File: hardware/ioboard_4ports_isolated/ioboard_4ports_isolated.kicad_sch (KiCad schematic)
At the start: 58 parts

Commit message: Finish IO-Board updates
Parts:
- C1, C10, C11, C12, C2, C3, C4, C5, C6, C7, C8, C9: value (none) -> 100nF; footprint (none) -> Capacitor_SMD:C_0603_1608Metric
- H1, H2, H3, H4: value (none) -> MountingHole; footprint (none) -> MountingHole:MountingHole_3.2mm_M3
- J1: value (none) -> Conn_02x06_Odd_Even; footprint (none) -> Connector_PinHeader_2.54mm:PinHeader_2x06_P2.54mm_Vertical
- J10, J2, J4, J8: value (none) -> XLR3; footprint (none) -> Connector_Audio:Jack_XLR_Neutrik_NC3FAAH_Horizontal
- J11, J3, J5, J9: value (none) -> XLR3; footprint (none) -> NC3FD-H:Jack_XLR_Neutrik_NC3FD-H_Horizontal
- J12, J13, J6, J7: value (none) -> Conn_01x03; footprint (none) -> Connector_PinHeader_2.54mm:PinHeader_1x03_P2.54mm_Vertical
- PS1, PS2: value (none) -> MEE1S0503SC; footprint (none) -> Converter_DCDC:Converter_DCDC_muRata_CRE1xxxxxx3C_THT
- R1, R11, R12, R17, R18, R2, R7, R8: value (none) -> 680R; footprint (none) -> Resistor_SMD:R_0603_1608Metric_Pad0.98x0.95mm_HandSolder
- R10, R19, R20, R9: value (none) -> 0R-DO_NOT_MOUNT; footprint (none) -> Resistor_SMD:R_0805_2012Metric_Pad1.20x1.40mm_HandSolder
- R13, R14, R3, R4: value (none) -> 0R; footprint (none) -> Resistor_SMD:R_0805_2012Metric_Pad1.20x1.40mm_HandSolder
- R15, R16, R5, R6: value (none) -> 120R; footprint (none) -> Resistor_SMD:R_0603_1608Metric_Pad0.98x0.95mm_HandSolder
- U1: value (none) -> M24C64-RMN6TP; footprint (none) -> Package_SO:SOIC-8_3.9x4.9mm_P1.27mm; LCSC C7562 -> C79988
- U2, U3: value (none) -> CRE1S0505DC; footprint (none) -> Converter_DCDC:Converter_DCDC_muRata_CRE1xxxxxxDC_THT
- U4, U5, U6, U7: value (none) -> ADM2483xRW; footprint (none) -> Package_SO:SOIC-16W_7.5x10.3mm_P1.27mm
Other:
- note added: "I2C EEPROM for board identification and configuration storage"
- note removed: "I2C EEPROM for board identification"

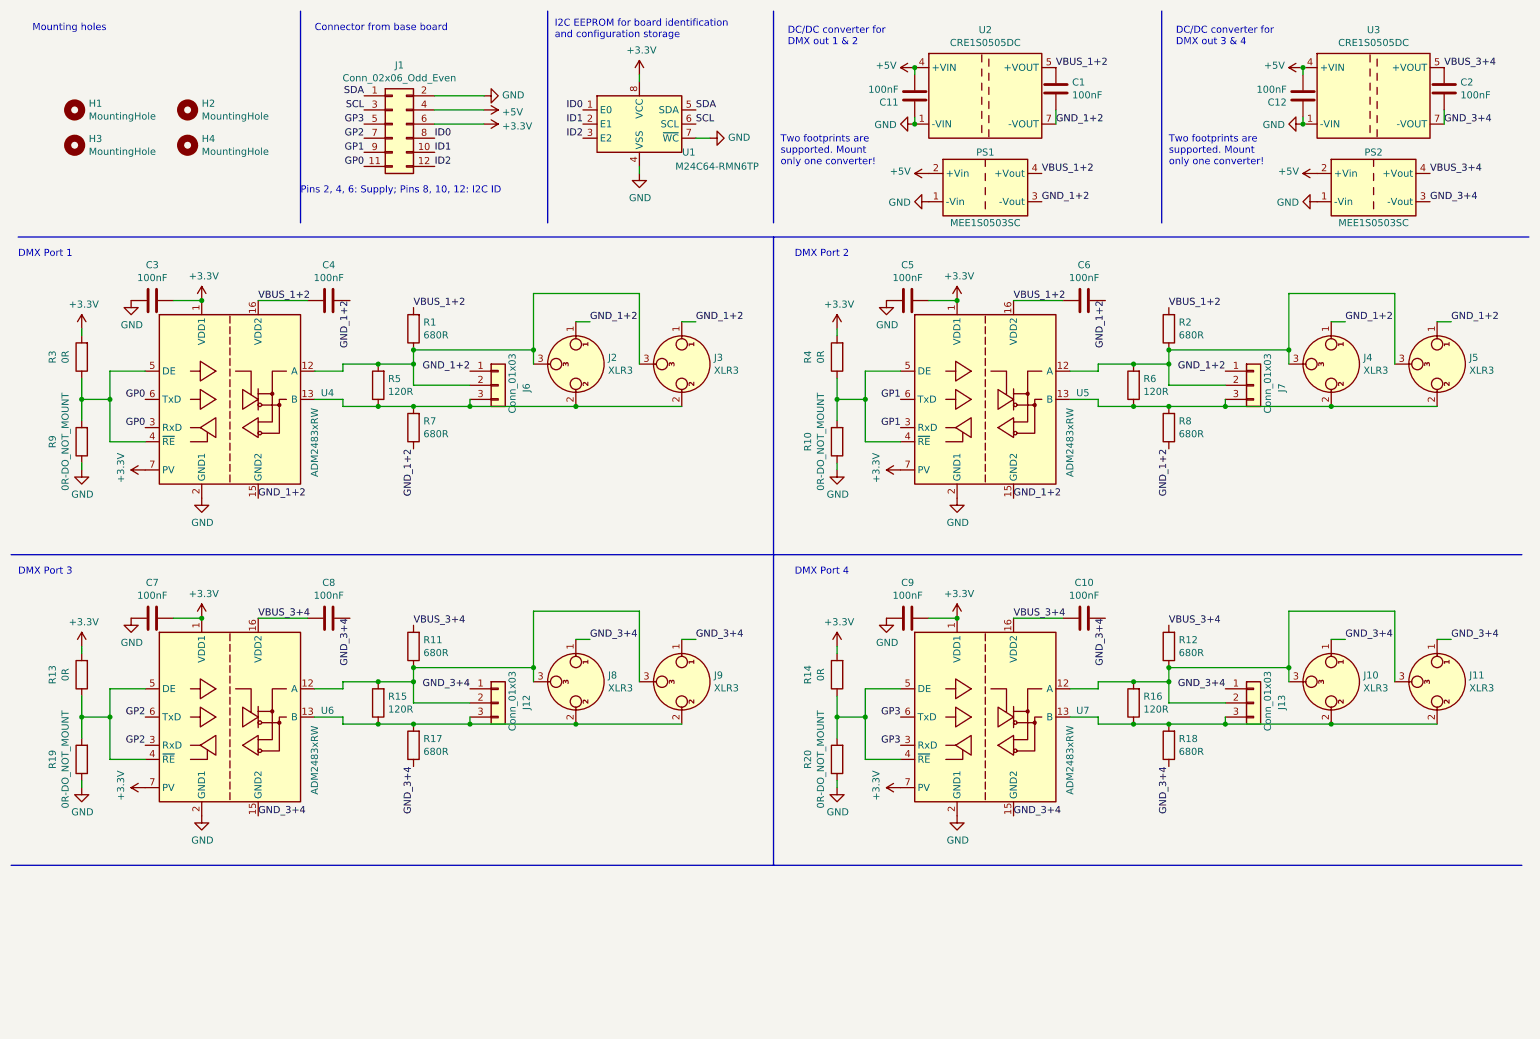
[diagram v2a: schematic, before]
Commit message: Add RJ45 jack to ioboard_4ports_isolated as well
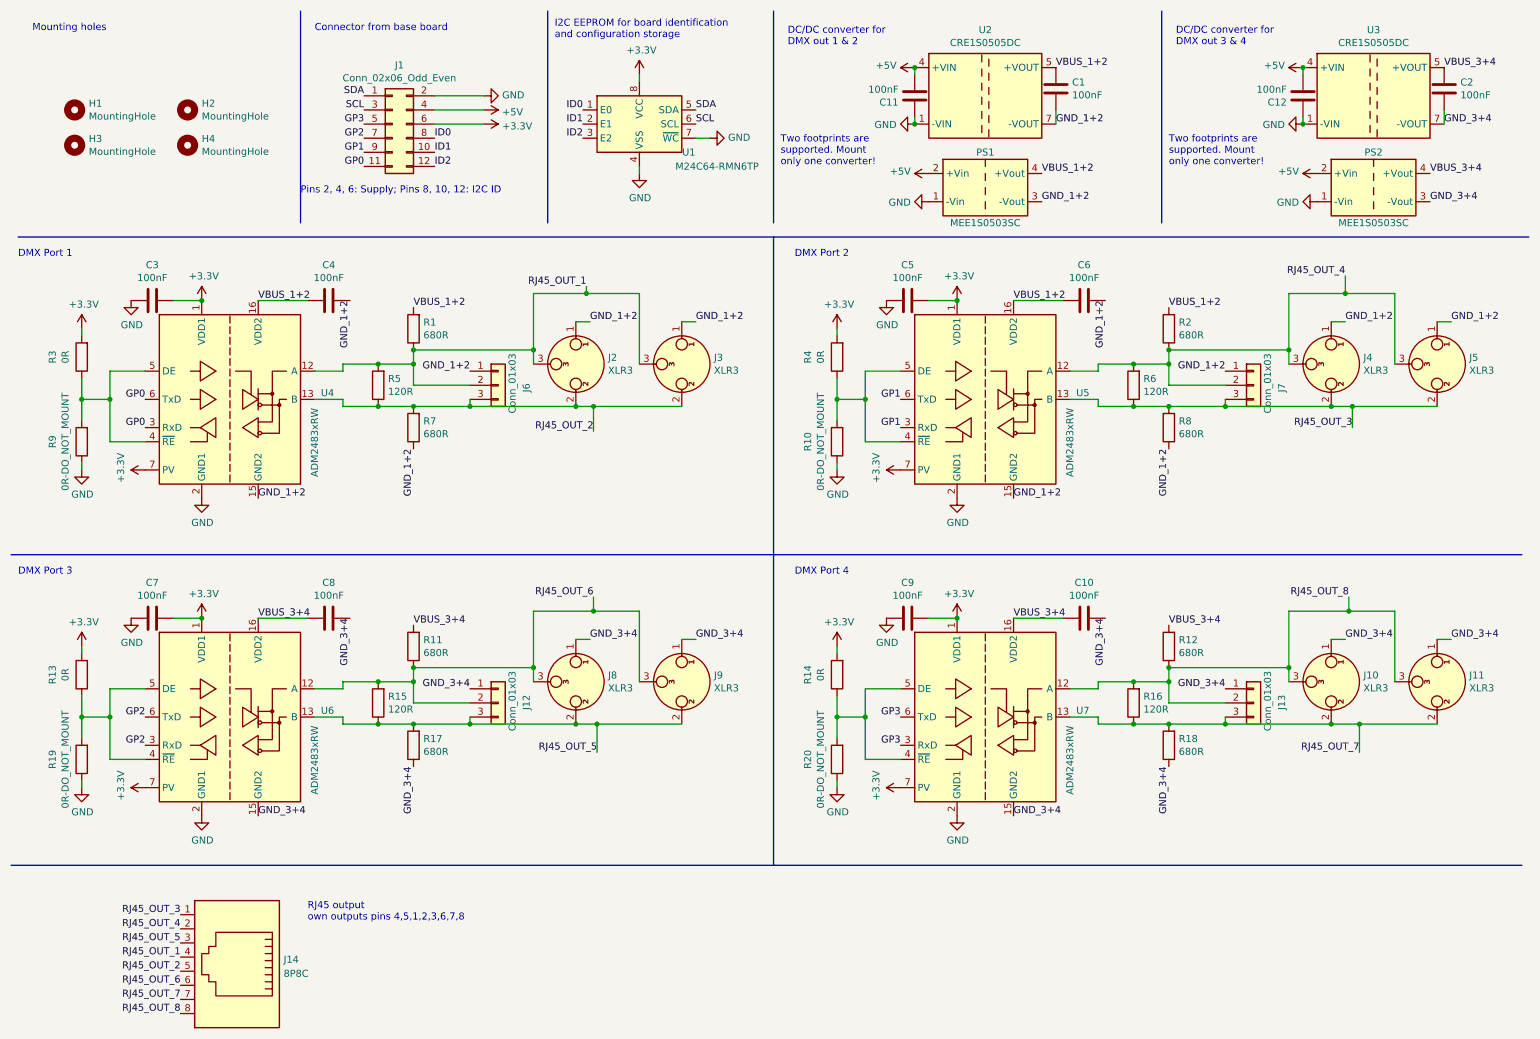
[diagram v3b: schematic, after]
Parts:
- added J14: 8P8C, RJ45_Sparkfun:RJ45_Sparkfun, symbol Connector:8P8C
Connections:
- net RJ45_OUT_1: now reaches J2.3, J3.3, J6.2 (Pin_2), R1.1, R5.2, U4.12 (A)
- net RJ45_OUT_1: now also J14.4
- net RJ45_OUT_2: now reaches J2.2, J3.2, J6.3 (Pin_3), R5.1, R7.2, U4.13 (B)
- net RJ45_OUT_2: now also J14.5
- net RJ45_OUT_5: now reaches J12.3 (Pin_3), J8.2, J9.2, R15.1, R17.2, U6.13 (B)
- net RJ45_OUT_5: now also J14.3
- net RJ45_OUT_6: now reaches J12.2 (Pin_2), J8.3, J9.3, R11.1, R15.2, U6.12 (A)
- net RJ45_OUT_6: now also J14.6
- net RJ45_OUT_7: now reaches J10.2, J11.2, J13.3 (Pin_3), R16.1, R18.2, U7.13 (B)
- net RJ45_OUT_7: now also J14.7
- net RJ45_OUT_8: now reaches J10.3, J11.3, J13.2 (Pin_2), R12.1, R16.2, U7.12 (A)
- net RJ45_OUT_8: now also J14.8
- net RJ45_OUT_3: now reaches J4.2, J5.2, J7.3 (Pin_3), R6.1, R8.2, U5.13 (B)
- net RJ45_OUT_3: now also J14.1
- net RJ45_OUT_4: now reaches J4.3, J5.3, J7.2 (Pin_2), R2.1, R6.2, U5.12 (A)
- net RJ45_OUT_4: now also J14.2
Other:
- note added: "RJ45 output own outputs pins 4,5,1,2,3,6,7,8"

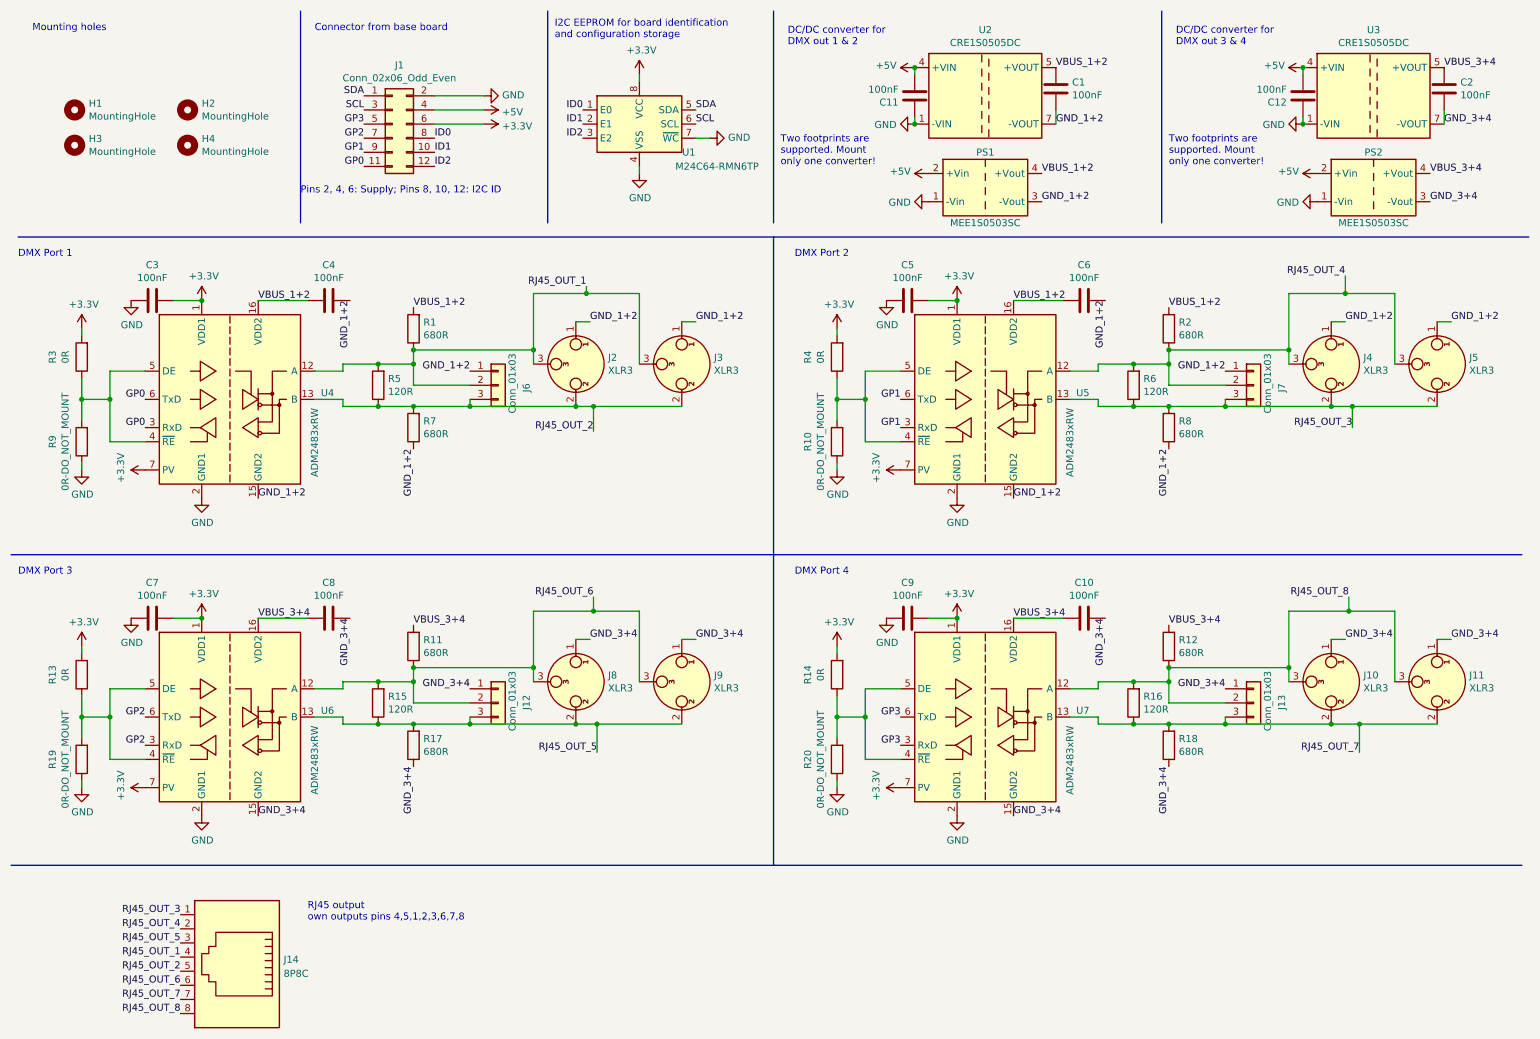
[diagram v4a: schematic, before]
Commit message: Update ioboards to KiCad 8, add OpenHardware logo
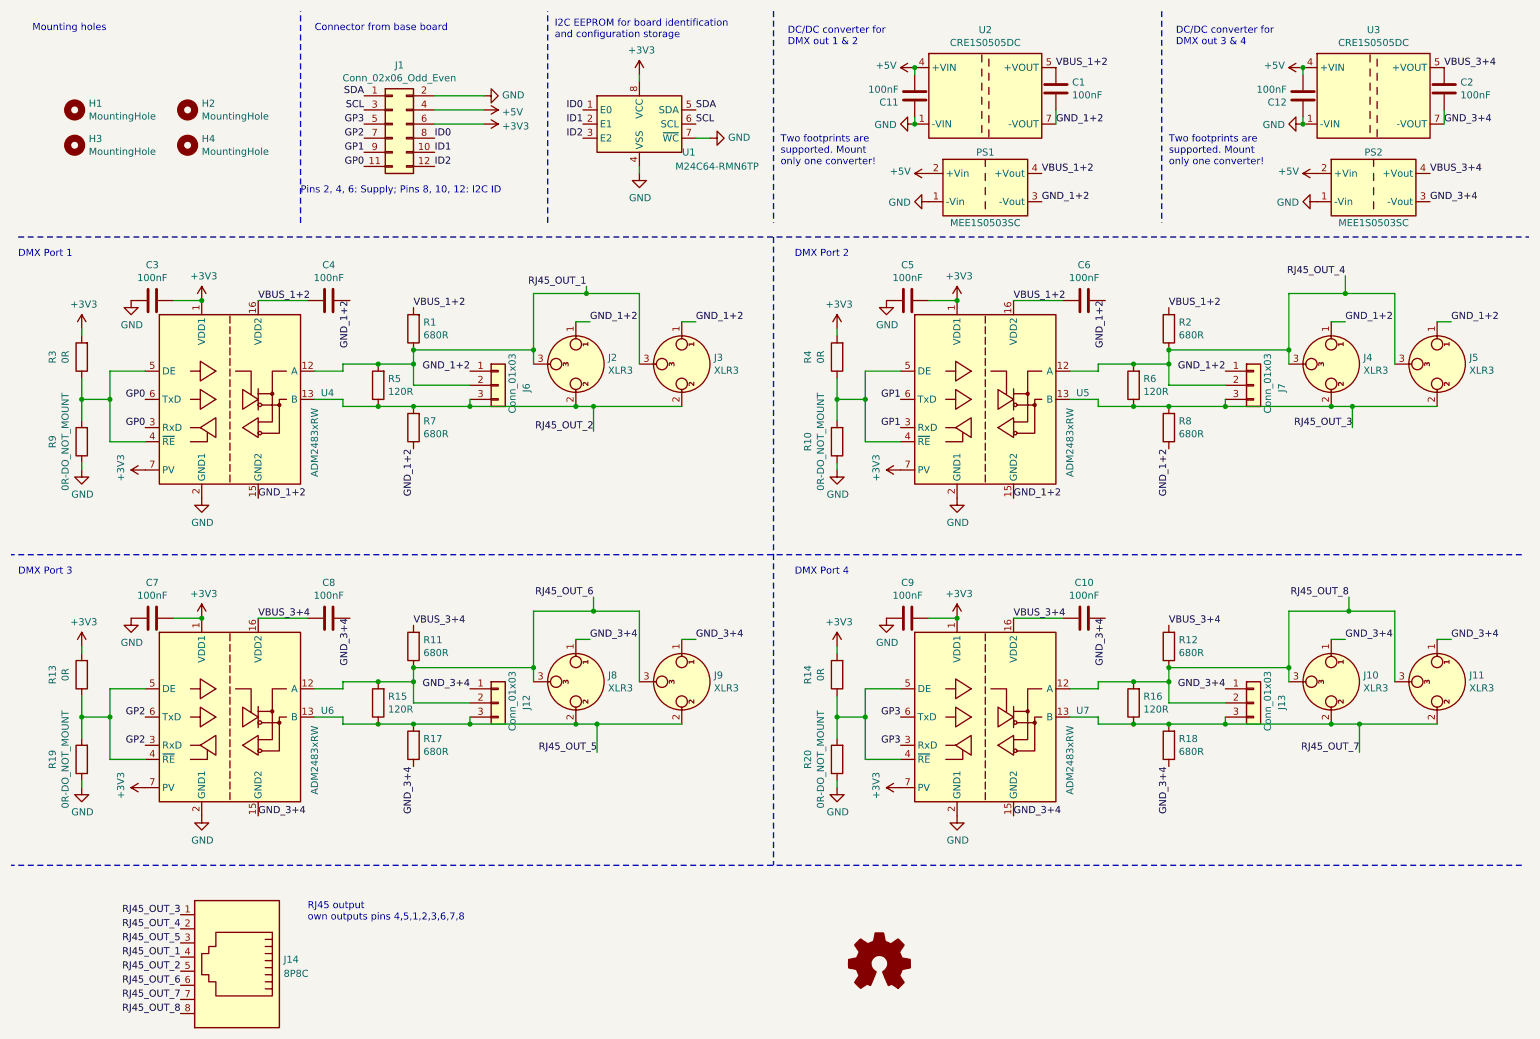
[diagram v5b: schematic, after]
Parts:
- added SYM1: Logo_Open_Hardware_Small, Symbol:OSHW-Logo2_7.3x6mm_SilkScreen, symbol Graphic:Logo_Open_Hardware_Small

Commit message: Update all footprints and ignore all other DRC warning on ioboards
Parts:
- PS1, PS2: footprint Converter_DCDC:Converter_DCDC_muRata_CRE1xxxxxx3C_THT -> Converter_DCDC:Converter_DCDC_Murata_CRE1xxxxxx3C_THT
- U2, U3: footprint Converter_DCDC:Converter_DCDC_muRata_CRE1xxxxxxDC_THT -> Converter_DCDC:Converter_DCDC_Murata_CRE1xxxxxxDC_THT
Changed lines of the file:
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@@
 			)
 		)
-		(property "Footprint" "Converter_DCDC:Converter_DCDC_muRata_CRE1xxxxxxDC_THT"
+		(property "Footprint" "Converter_DCDC:Converter_DCDC_Murata_CRE1xxxxxxDC_THT"
 			(at 186.69 36.83 0)
 			(effects
@@
 			)
 		)
-		(property "Footprint" "Converter_DCDC:Converter_DCDC_muRata_CRE1xxxxxx3C_THT"
+		(property "Footprint" "Converter_DCDC:Converter_DCDC_Murata_CRE1xxxxxx3C_THT"
 			(at 160.02 50.8 0)
 			(effects
@@
 			)
 		)
-		(property "Footprint" "Converter_DCDC:Converter_DCDC_muRata_CRE1xxxxxx3C_THT"
+		(property "Footprint" "Converter_DCDC:Converter_DCDC_Murata_CRE1xxxxxx3C_THT"
 			(at 229.87 50.8 0)
 			(effects
@@
 			)
 		)
-		(property "Footprint" "Converter_DCDC:Converter_DCDC_muRata_CRE1xxxxxxDC_THT"
+		(property "Footprint" "Converter_DCDC:Converter_DCDC_Murata_CRE1xxxxxxDC_THT"
 			(at 256.54 36.83 0)
 			(effects
@@
 			(at 167.64 184.15 0)
 			(effects
-				(font
-					(size 1.27 1.27)
-				)
-				(hide yes)
-			)
-		)
-		(property "Sim.Enable" "0"
-			(at 167.64 184.15 0)
-			(effects
